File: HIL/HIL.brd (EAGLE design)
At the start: 129.1 x 103.7 mm, 247 parts, among them J1 JTAG_ARM_10PIN, J4 JTAG_ARM_10PIN, U1 CD74HC4067SM96, U10 INA219AIDCNR, U11 INA219AIDCNR, U12 INA219AIDCNR, U14 ADUM1201ARZ, U15 SN65HVD230D, U16 TL1963AKTTR., U17 FT230XS, U2 TL1963AKTTR., U3 CD74HC4067SM96, U4 CD74HC4067SM96, U5 MCP4725A0T-E/CH, U6 TL1963AKTTR., U7 MCP2003-E/SN, U8 TM4C1294NCPDT, U9 INA219AIDCNR, X1 A1944-50, X2 A1944-50, X4 A1944-50, Y3 NX3225GA

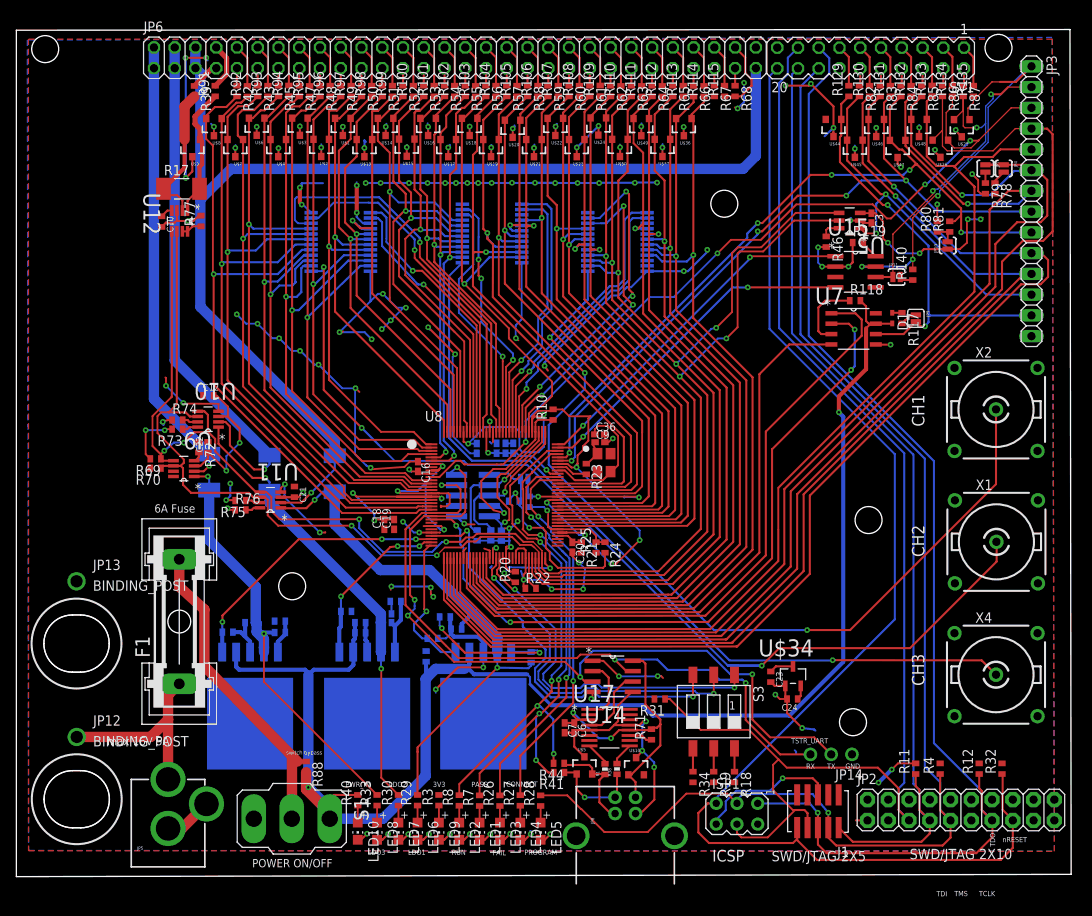
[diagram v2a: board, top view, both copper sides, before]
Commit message: Change:  - MCU to a proper package Add:        - labels                 - i2c header                 - UART header
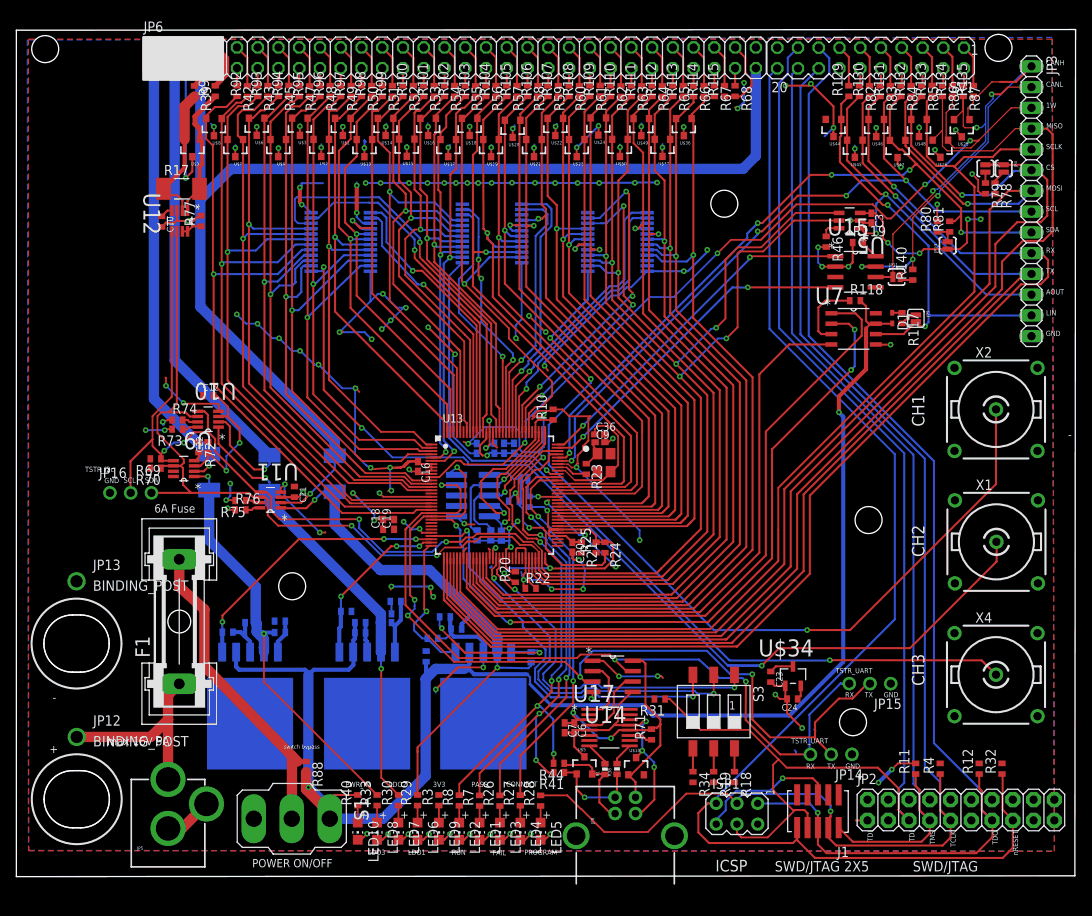
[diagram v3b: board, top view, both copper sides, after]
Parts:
- removed U8: TM4C1294NCPDT, MRDT-Microcontrollers:TQFP-128
- added JP15, JP16: (no value), JDT-1800_smahed:1X03-CLEANBIG
- added U13: TM4C1294NCPDT, ti-tiva:TQFP128
- R26, R27, R28, R29, R3, R30, R33, R40, R7, R8: value (none) -> 100R
- moved C13 0.28 mm to (58.5, 52.7)
- moved C14 0.18 mm to (59.7, 52.7)
- moved C18 0.15 mm to (44.9, 43.3)
- moved C15 0.10 mm to (60.9, 52.7)
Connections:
- removed net N_$24: R20.1, U8.P$64
- removed net N_$33: C37.1, R24.1, R25.2, U8.P$70
- net AD0: now also U13.21; no longer U8.P$21
- net AD1: now also U13.20; no longer U8.P$20
- net AD10: now also U13.2; no longer U8.P$2
- net AD11: now also U13.1; no longer U8.P$1
- net AD12: now also U13.128; no longer U8.P$128
- net AD13: now also U13.127; no longer U8.P$127
- net AD14: now also U13.126; no longer U8.P$126
- net AD15: now also U13.125; no longer U8.P$125
- net AD16: now also U13.124; no longer U8.P$124
- net AD17: now also U13.123; no longer U8.P$123
- net AD18: now also U13.121; no longer U8.P$121
- net AD19: now also U13.120; no longer U8.P$120
- net AD2: now also U13.19; no longer U8.P$19
- net AD3: now also U13.18; no longer U8.P$18
- net AD4: now also U13.15; no longer U8.P$15
- net AD5: now also U13.14; no longer U8.P$14
- net AD6: now also U13.13; no longer U8.P$13
- net AD7: now also U13.12; no longer U8.P$12
- net AD8: now also U13.4; no longer U8.P$4
- net AD9: now also U13.3; no longer U8.P$3
- net CAN_RX: now also U13.95; no longer U8.P$95
- net CAN_TX: now also U13.96; no longer U8.P$96
- net D0: now also U13.112; no longer U8.P$112
- net D1: now also U13.111; no longer U8.P$111
- net D10: now also U13.77; no longer U8.P$77
- net D11: now also U13.76; no longer U8.P$76
- net D12: now also U13.75; no longer U8.P$75
- net D13: now also U13.74; no longer U8.P$74
- net D14: now also U13.73; no longer U8.P$73
- net D15: now also U13.72; no longer U8.P$72
- net D16: now also U13.71; no longer U8.P$71
- net D19: now also U13.61; no longer U8.P$61
- net D2: now also U13.5; no longer U8.P$5
- net D20: now also U13.60; no longer U8.P$60
- net D21: now also U13.46; no longer U8.P$46
- net D22: now also U13.45; no longer U8.P$45
- net D23: now also U13.44; no longer U8.P$44
- net D24: now also U13.43; no longer U8.P$43
- net D25: now also U13.42; no longer U8.P$42
- net D3: now also U13.6; no longer U8.P$6
- net D4: now also U13.102; no longer U8.P$102
- net D5: now also U13.84; no longer U8.P$84
- net D6: now also U13.83; no longer U8.P$83
- net D7: now also U13.82; no longer U8.P$82
- net D8: now also U13.81; no longer U8.P$81
- net D9: now also U13.78; no longer U8.P$78
- net DUT_CONNECT: now also U13.85; no longer U8.P$85
- net DUT_CS: now also U13.36; no longer U8.P$36
- net DUT_MISO: now also U13.35; no longer U8.P$35
- net DUT_MOSI: now also U13.37; no longer U8.P$37
- net DUT_ONEWIRE: now also U13.11; no longer U8.P$11
- net DUT_RX: now also U13.33; no longer U8.P$33
- net DUT_SCL: now also U13.91; no longer U8.P$91
- net DUT_SCLK: now also U13.38; no longer U8.P$38
- net DUT_SDA: now also U13.92; no longer U8.P$92
- net DUT_TX: now also U13.34; no longer U8.P$34
- net GND: now also JP15.1, JP16.1, U13.10, U13.114, U13.17, U13.48, U13.55, U13.58, U13.80; no longer U8.P$10, U8.P$114, U8.P$17, U8.P$48, U8.P$55, U8.P$58, U8.P$80
- net LDO1_ENABLE: now also U13.32; no longer U8.P$32
- net LDO2_ENABLE: now also U13.31; no longer U8.P$31
- net LDO3_ENABLE: now also U13.30; no longer U8.P$30
- net LIN_CS: now also U13.24; no longer U8.P$24
- net LIN_RX: now also U13.40; no longer U8.P$40
- net LIN_TX: now also U13.41; no longer U8.P$41
- net M0S0: now also U13.107; no longer U8.P$107
- net M0S1: now also U13.108; no longer U8.P$108
- net M0S2: now also U13.109; no longer U8.P$109
- net M0S3: now also U13.110; no longer U8.P$110
- net M1S0: now also U13.116; no longer U8.P$116
- net M1S1: now also U13.117; no longer U8.P$117
- net M1S2: now also U13.119; no longer U8.P$119
- net M1S3: now also U13.118; no longer U8.P$118
- net M2S0: now also U13.103; no longer U8.P$103
- net M2S1: now also U13.104; no longer U8.P$104
- net M2S2: now also U13.105; no longer U8.P$105
- net M2S3: now also U13.106; no longer U8.P$106
- net N_$2: now also C37.1, R20.1, R24.1, R25.2, U13.64, U13.68, U13.70; no longer U8.P$68
- net N_$28: now also U13.115, U13.87; no longer U8.P$115, U8.P$87
- net N_$29: now also U13.59; no longer U8.P$59
- net N_$30: now also U13.89; no longer U8.P$89
- net N_$31: now also U13.88; no longer U8.P$88
- net PC4: now also U13.25; no longer U8.P$25
- net SW1: now also U13.29; no longer U8.P$29
- net SW2: now also U13.49; no longer U8.P$49
- net SW3: now also U13.50; no longer U8.P$50
- net TARGET_TCK/SWCLK: now also U13.100; no longer U8.P$100
- net TARGET_TDI: now also U13.98; no longer U8.P$98
- net TARGET_TDO/SWO: now also U13.97; no longer U8.P$97
- net TARGET_TMS/SWDIO: now also U13.99; no longer U8.P$99
- net TEST_FAIL: now also U13.86; no longer U8.P$86
- net TEST_PASS: now also U13.93; no longer U8.P$93
- net TEST_RUN: now also U13.94; no longer U8.P$94
- net TSTR_3V3: now also U13.101, U13.113, U13.122, U13.16, U13.26, U13.28, U13.39, U13.47, U13.51, U13.52, U13.69, U13.7, U13.79, U13.8, U13.9, U13.90; no longer U8.P$101, U8.P$113, U8.P$122, U8.P$16, U8.P$26, U8.P$28, U8.P$39, U8.P$47, U8.P$51, U8.P$52, U8.P$69, U8.P$7, U8.P$79, U8.P$8, U8.P$9, U8.P$90
- net TSTR_RX: now also JP15.3, U13.22; no longer U8.P$22
- net TSTR_SCL: now also JP16.2, U13.63; no longer U8.P$63
- net TSTR_SDA: now also JP16.3, U13.62; no longer U8.P$62
- net TSTR_TX: now also JP15.2, U13.23; no longer U8.P$23
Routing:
- net N_$2: track 4.47 -> 40.3 mm, vias 0 -> 3
- net TSTR_3V3: track 357.8 -> 326.1 mm
- net GND: track 333.1 -> 319.3 mm, vias 82 -> 84
- net N_$33: track 12.6 -> 0.00 mm, vias 1 -> 0
- net TSTR_RX: track 86.8 -> 98.3 mm
- net TSTR_TX: track 94.6 -> 105.3 mm
- net N_$24: track 9.27 -> 0.00 mm, vias 2 -> 0
- net TSTR_SCL: track 210.1 -> 218.3 mm
- net TSTR_SDA: track 209.8 -> 214.6 mm
- net D11: track 72.6 -> 74.2 mm
- net N_$28: track 12.2 -> 13.7 mm
- net M0S0: track 33.1 -> 34.5 mm
- net D12: track 75.1 -> 76.2 mm
- net D13: track 75.1 -> 76.2 mm
- net M1S1: track 42.2 -> 43.1 mm
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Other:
- board size 129.1 x 103.7 mm -> 129.6 x 103.7 mm
- board text added: "+"
- board text added: "-"
- board text added: "1W"
- board text added: "AOUT"
- board text added: "Analog(A0-A19)"
- board text added: "CANH"
- board text added: "CANL"
- board text added: "CS"
- board text added: "Communication"
- board text added: "Digital(D0-D25)"
- board text added: "JTAG"
- board text added: "LIN"
- board text added: "MISO"
- board text added: "MOSI"
- board text added: "Power"
- board text added: "SCL"
- board text added: "SCLK"
- board text added: "SDA"
- board text added: "SWD/JTAG"
- board text added: "TSTR_i2c"
- board text removed: "SWD/JTAG 2X10"

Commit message: change the position of the holes fix component libaries
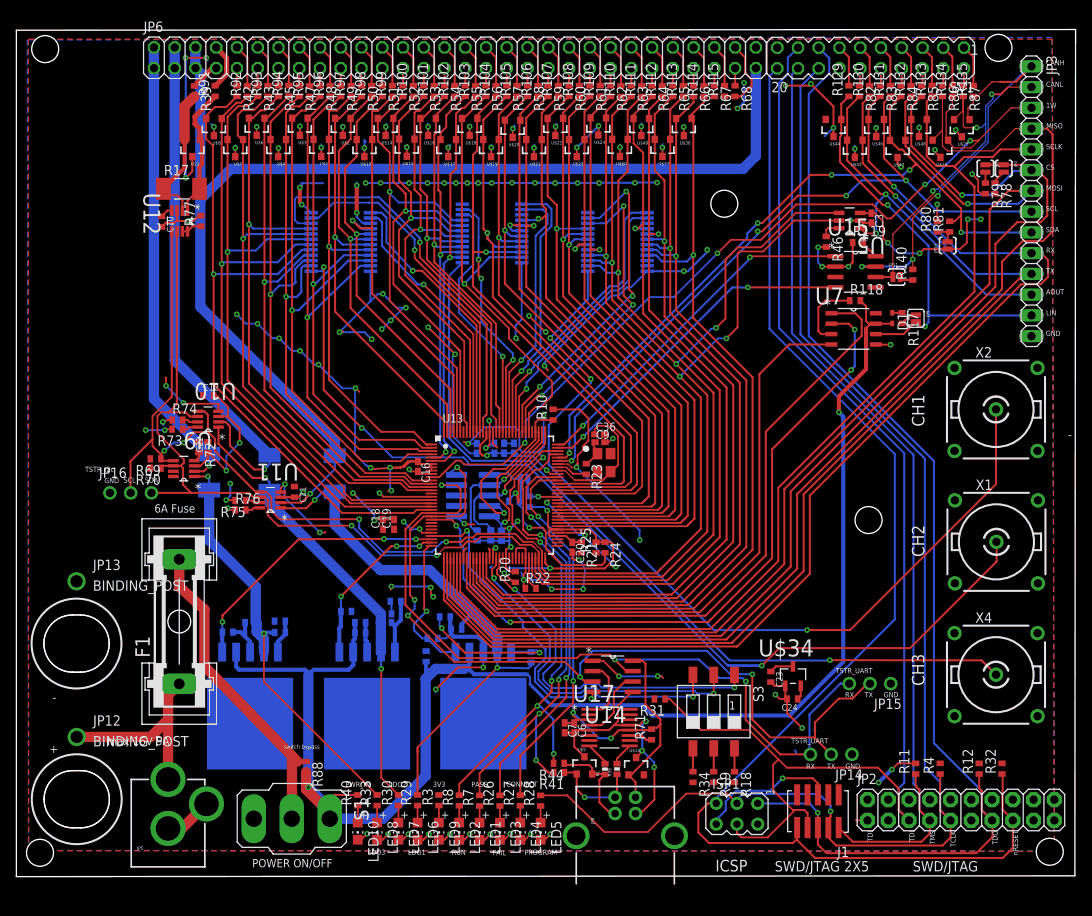
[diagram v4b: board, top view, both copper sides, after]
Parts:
- moved STANDOFF1 44.9 mm to (2.90, 3.15)
- moved STANDOFF6 28.8 mm to (126.5, 3.28)
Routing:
- net TSTR_3V3: track 326.1 -> 321.6 mm
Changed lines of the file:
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@@
 <wire x1="116.967" y1="95.5802" x2="116.967" y2="95.7326" width="0.254" layer="21"/>
 <text x="73.5584" y="95.7834" size="1.27" layer="22" font="vector" rot="MR0">Digital(D0-D25)</text>
-<text x="98.1202" y="94.5896" size="1.27" layer="22" font="vector" rot="MR0">JTAG</text>
-<text x="116.5098" y="95.7326" size="1.27" layer="22" font="vector" rot="MR0">Communication</text>
-<polygon width="0.254" layer="21">
+<text x="97.9424" y="95.0722" size="1.27" layer="22" font="vector" rot="MR0">JTAG</text>
+<text x="115.6716" y="95.4278" size="1.27" layer="22" font="vector" rot="MR0">Communication</text>
+<polygon width="0.254" layer="22">
 <vertex x="15.5448" y="102.9716"/>
 <vertex x="25.2984" y="102.9716"/>
@@
 <vertex x="15.5194" y="102.9462"/>
 </polygon>
-<text x="23.0378" y="96.0882" size="1.27" layer="22" font="vector" rot="MR0">Power</text>
+<text x="21.9202" y="96.0374" size="1.27" layer="22" font="vector" rot="MR0">Power</text>
 </plain>
 <attributes>
@@
 <element name="U$5" library="SparkFun-DiscreteSemi" package="SOT23-3" value="zener_3.3V" x="69.5198" y="13.7922"/>
 <element name="U$10" library="SparkFun-DiscreteSemi" package="SOT23-3" value="zener_3.3V" x="75.8444" y="13.6906"/>
-<element name="STANDOFF1" library="SparkFun-Electromechanical" package="STAND-OFF" value="STAND-OFF" x="33.7566" y="35.7632"/>
+<element name="STANDOFF1" library="SparkFun-Electromechanical" package="STAND-OFF" value="STAND-OFF" x="2.8956" y="3.1496"/>
 <element name="STANDOFF2" library="SparkFun-Electromechanical" package="STAND-OFF" value="STAND-OFF" x="120.1928" y="101.6508"/>
 <element name="STANDOFF5" library="SparkFun-Electromechanical" package="STAND-OFF" value="STAND-OFF" x="86.6394" y="82.5754"/>
-<element name="STANDOFF6" library="SparkFun-Electromechanical" package="STAND-OFF" value="STAND-OFF" x="102.3874" y="19.1262"/>
+<element name="STANDOFF6" library="SparkFun-Electromechanical" package="STAND-OFF" value="STAND-OFF" x="126.4666" y="3.2766"/>
 <element name="R72" library="resistor" package="R0402" value="4k7" x="22.3266" y="52.7812" rot="R270"/>
 <element name="R73" library="resistor" package="R0402" value="4k7" x="19.7104" y="54.991" rot="R180"/>
@@
 <wire x1="55.2958" y1="53.213" x2="56.3214" y2="53.213" width="0.2286" layer="16"/>
 <wire x1="56.3214" y1="53.213" x2="56.3372" y2="53.2288" width="0.2286" layer="16"/>
-<wire x1="63.125" y1="56.5464" x2="63.8048" y2="57.2262" width="0.2286" layer="1"/>
-<wire x1="63.8048" y1="57.2262" x2="65.4916" y2="57.2262" width="0.2286" layer="1"/>
 <wire x1="65.4916" y1="57.2262" x2="65.6844" y2="57.419" width="0.2286" layer="1"/>
 <wire x1="59.9186" y1="38.1" x2="59.9186" y2="39.1918" width="0.2286" layer="1"/>
@@
 <wire x1="37.1348" y1="42.3418" x2="37.7952" y2="42.3418" width="0.2286" layer="1"/>
 <wire x1="37.7952" y1="42.3418" x2="37.8206" y2="42.3672" width="0.2286" layer="1"/>
-<wire x1="63.125" y1="56.2162" x2="63.4492" y2="56.5404" width="0.2286" layer="1"/>
-<wire x1="63.4492" y1="56.5404" x2="64.2874" y2="56.5404" width="0.2286" layer="1"/>
 <wire x1="64.2874" y1="56.5404" x2="64.5414" y2="56.7944" width="0.2286" layer="1"/>
 <via x="64.5414" y="56.7944" extent="1-16" drill="0.3048"/>
@@
 <wire x1="69.342" y1="52.9082" x2="70.0024" y2="53.5686" width="0.2286" layer="1"/>
 <wire x1="70.0024" y1="53.5686" x2="70.0024" y2="56.3118" width="0.2286" layer="1"/>
-<wire x1="70.0024" y1="56.3118" x2="70.2564" y2="56.5658" width="0.2286" layer="1"/>
-<wire x1="70.2564" y1="56.5658" x2="67.6656" y2="56.5658" width="0.2286" layer="1"/>
-<wire x1="67.6656" y1="56.5658" x2="66.8274" y2="57.404" width="0.2286" layer="1"/>
 <wire x1="66.8274" y1="57.404" x2="65.6994" y2="57.404" width="0.2286" layer="1"/>
 <wire x1="65.6994" y1="57.404" x2="65.6844" y2="57.419" width="0.2286" layer="1"/>
@@
 <wire x1="58.3216" y1="54.6388" x2="58.3216" y2="53.2352" width="0.2286" layer="1"/>
 <wire x1="58.3216" y1="53.2352" x2="58.8264" y2="52.7304" width="0.254" layer="1"/>
+<wire x1="66.8274" y1="57.404" x2="68.9102" y2="57.404" width="0.254" layer="1"/>
+<wire x1="68.9102" y1="57.404" x2="70.0024" y2="56.3118" width="0.254" layer="1"/>
 </signal>
 <signal name="LDO1_SH+" class="5">
